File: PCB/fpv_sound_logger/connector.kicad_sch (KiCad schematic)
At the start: 18 parts, among them CN1 SM04B-SRSS-TB(LF)(SN), J2 MSD-4-A, U3 TLV75533PDBVR

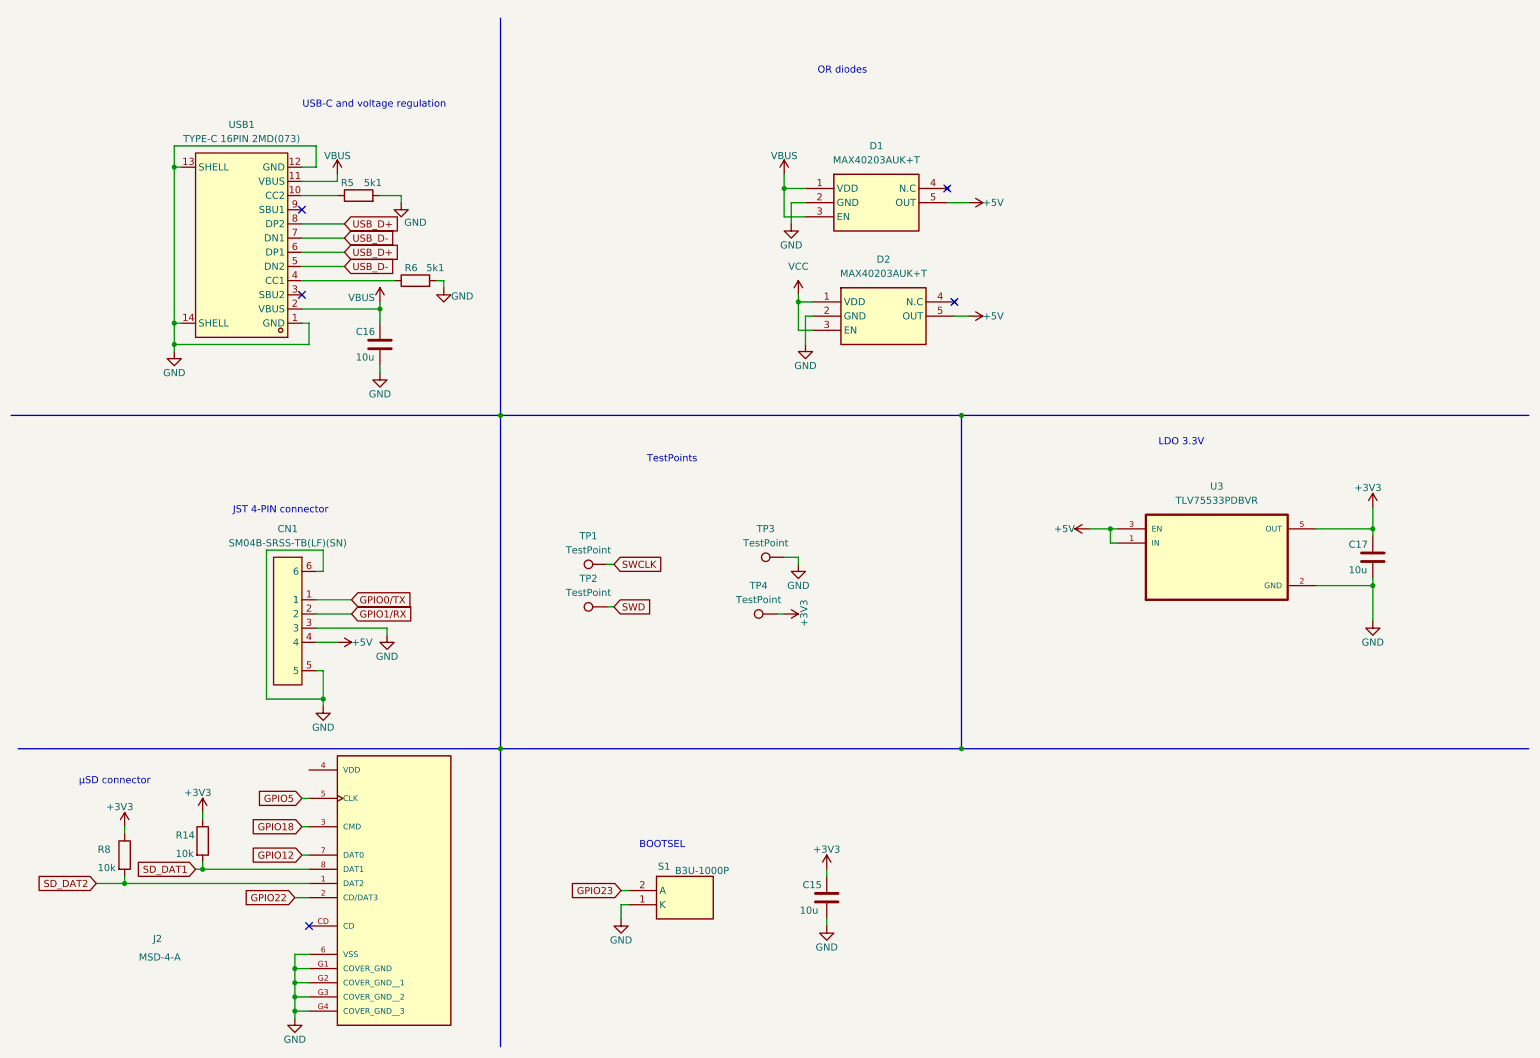
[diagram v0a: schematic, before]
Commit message: place new components and started routing for v2
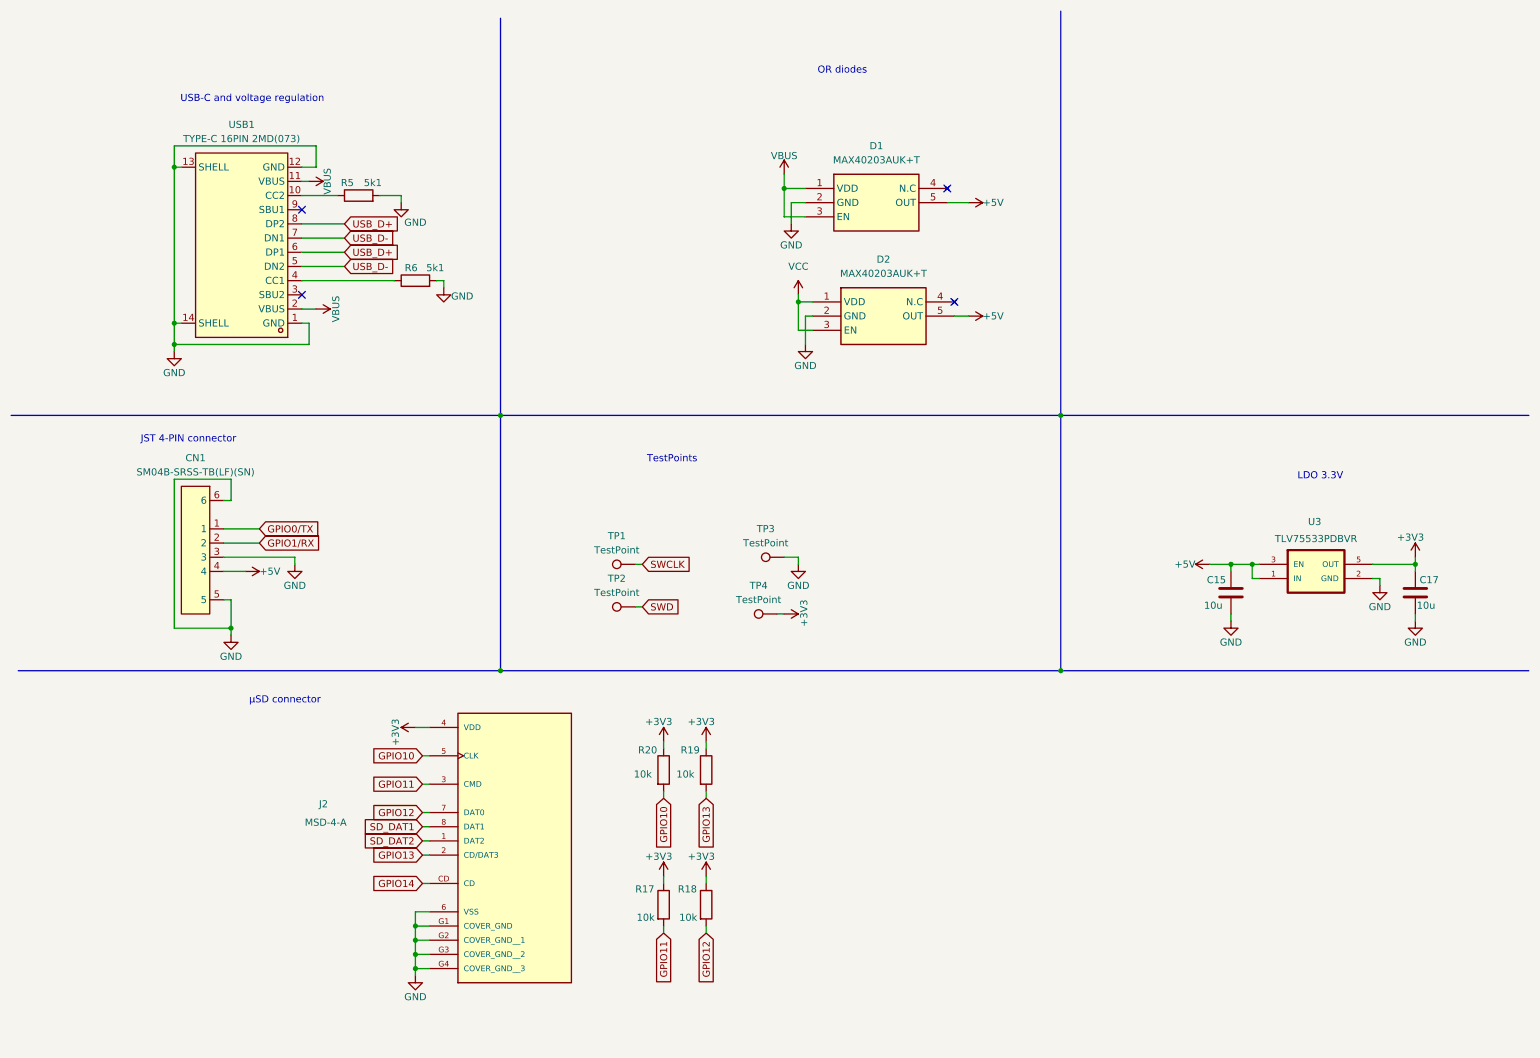
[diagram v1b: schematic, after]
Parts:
- removed C16: 10u, Capacitor_SMD:C_0805_2012Metric, symbol Device:C
- removed R14, R8: 10k, symbol Device:R
- removed S1: B3U-1000P, fpv_sound_logger:B3U-1000P, symbol SoundLogger:B3U-1000P
- added R17, R18, R19, R20: 10k, Resistor_SMD:R_0805_2012Metric, symbol Device:R
- R5, R6: footprint Capacitor_SMD:C_0805_2012Metric -> Resistor_SMD:R_0805_2012Metric
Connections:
- net +3V3: now also J2.4 (VDD), R17.1, R18.1, R19.1, R20.1; no longer C15.1
- net +5V: now also C15.1
- net GPIO12: now also R18.2
- net GPIO14: now reaches J2.CD
- net GPIO18 renamed GPIO11
- net GPIO11: now also R17.2
- net GPIO22 renamed GPIO13
- net GPIO13: now also R19.2
- net GPIO5 renamed GPIO10
- net GPIO10: now also R20.2
- no-connect marks 5 -> 4
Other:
- note removed: "BOOTSEL"
- moved on the sheet: C17, CN1, J2, TP1, TP2, U3

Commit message: Update component footprints and add manufacturer details in sensor schematic
- Changed resistor footprint from R_0805 to R_0603 for multiple components.
- Updated manufacturer part numbers, manufacturers, suppliers, and supplier parts for various components.
- Added manufacturer and supplier information for OMRON components.
- Removed outdated datasheet link and replaced with relevant part numbers for clarity.
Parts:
- C15, C17: footprint Capacitor_SMD:C_0805_2012Metric -> Capacitor_SMD:C_0603_1608Metric; MANUFACTURER (none) -> Samsung Electro-Mechanics; Manufacturer_Part_Number (none) -> CL10A106MQ8NNNC; Supplier (none) -> LCSC; Supplier Part (none) -> C1691
- CN1: MANUFACTURER (none) -> JST; Manufacturer JST -> (none)
- D1, D2: MANUFACTURER (none) -> MAXIM; Supplier (none) -> LCSC; Supplier Part (none) -> C2653639
- J2: Manufacturer_Part_Number (none) -> MSD-4-A; Supplier (none) -> LCSC; Supplier Part (none) -> C22367949
- R17, R18, R19, R20: footprint Resistor_SMD:R_0805_2012Metric -> Resistor_SMD:R_0603_1608Metric; MANUFACTURER (none) -> PANASONIC; Manufacturer_Part_Number (none) -> ERJUP3F1002V; Supplier (none) -> LCSC; Supplier Part (none) -> ERJUP3F1002V
- R5, R6: footprint Resistor_SMD:R_0805_2012Metric -> Resistor_SMD:R_0603_1608Metric; MANUFACTURER (none) -> PANASONIC; Manufacturer_Part_Number (none) -> ERA3AEB512V; Supplier (none) -> LCSC; Supplier Part (none) -> ERA3AEB512V
- TP1, TP2, TP3, TP4: now not fitted; now left out of the parts list
- U3: MANUFACTURER (none) -> TI; Manufacturer_Part_Number (none) -> TLV75533PDBVR; Supplier (none) -> LCSC; Supplier Part (none) -> C404027
- USB1: Manufacturer SHOU HAN(首韩) -> (none)

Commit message: Refactor code structure for improved readability and maintainability
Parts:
- TP1, TP2, TP3, TP4: now in the parts list
- USB1: MANUFACTURER (none) -> SHOU HAN
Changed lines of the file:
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@@
 		(body_style 1)
 		(exclude_from_sim no)
-		(in_bom no)
+		(in_bom yes)
 		(on_board yes)
 		(in_pos_files yes)
@@
 		(body_style 1)
 		(exclude_from_sim no)
-		(in_bom no)
+		(in_bom yes)
 		(on_board yes)
 		(in_pos_files yes)
@@
 			)
 		)
+		(property "MANUFACTURER" "SHOU HAN"
+			(at 53.34 54.61 0)
+			(hide yes)
+			(show_name no)
+			(do_not_autoplace no)
+			(effects
+				(font
+					(size 1.27 1.27)
+				)
+			)
+		)
 		(pin "8"
 		)
@@
 		(body_style 1)
 		(exclude_from_sim no)
-		(in_bom no)
+		(in_bom yes)
 		(on_board yes)
 		(in_pos_files yes)
@@
 		(body_style 1)
 		(exclude_from_sim no)
-		(in_bom no)
+		(in_bom yes)
 		(on_board yes)
 		(in_pos_files yes)
